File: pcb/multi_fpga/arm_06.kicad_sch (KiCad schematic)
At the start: 16 parts, among them U49 IM72D128V01XTMA1, U50 IM72D128V01XTMA1, U51 IM72D128V01XTMA1, U52 IM72D128V01XTMA1, U53 IM72D128V01XTMA1, U54 IM72D128V01XTMA1, U55 IM72D128V01XTMA1, U56 IM72D128V01XTMA1

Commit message: Fixed library and power issues.
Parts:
- C49, C50, C51, C52, C53, C54, C55, C56: symbol C -> multi_fpga:C
- U49, U50, U51, U52, U53, U54, U55, U56: symbol IM72D128 -> multi_fpga:IM72D128

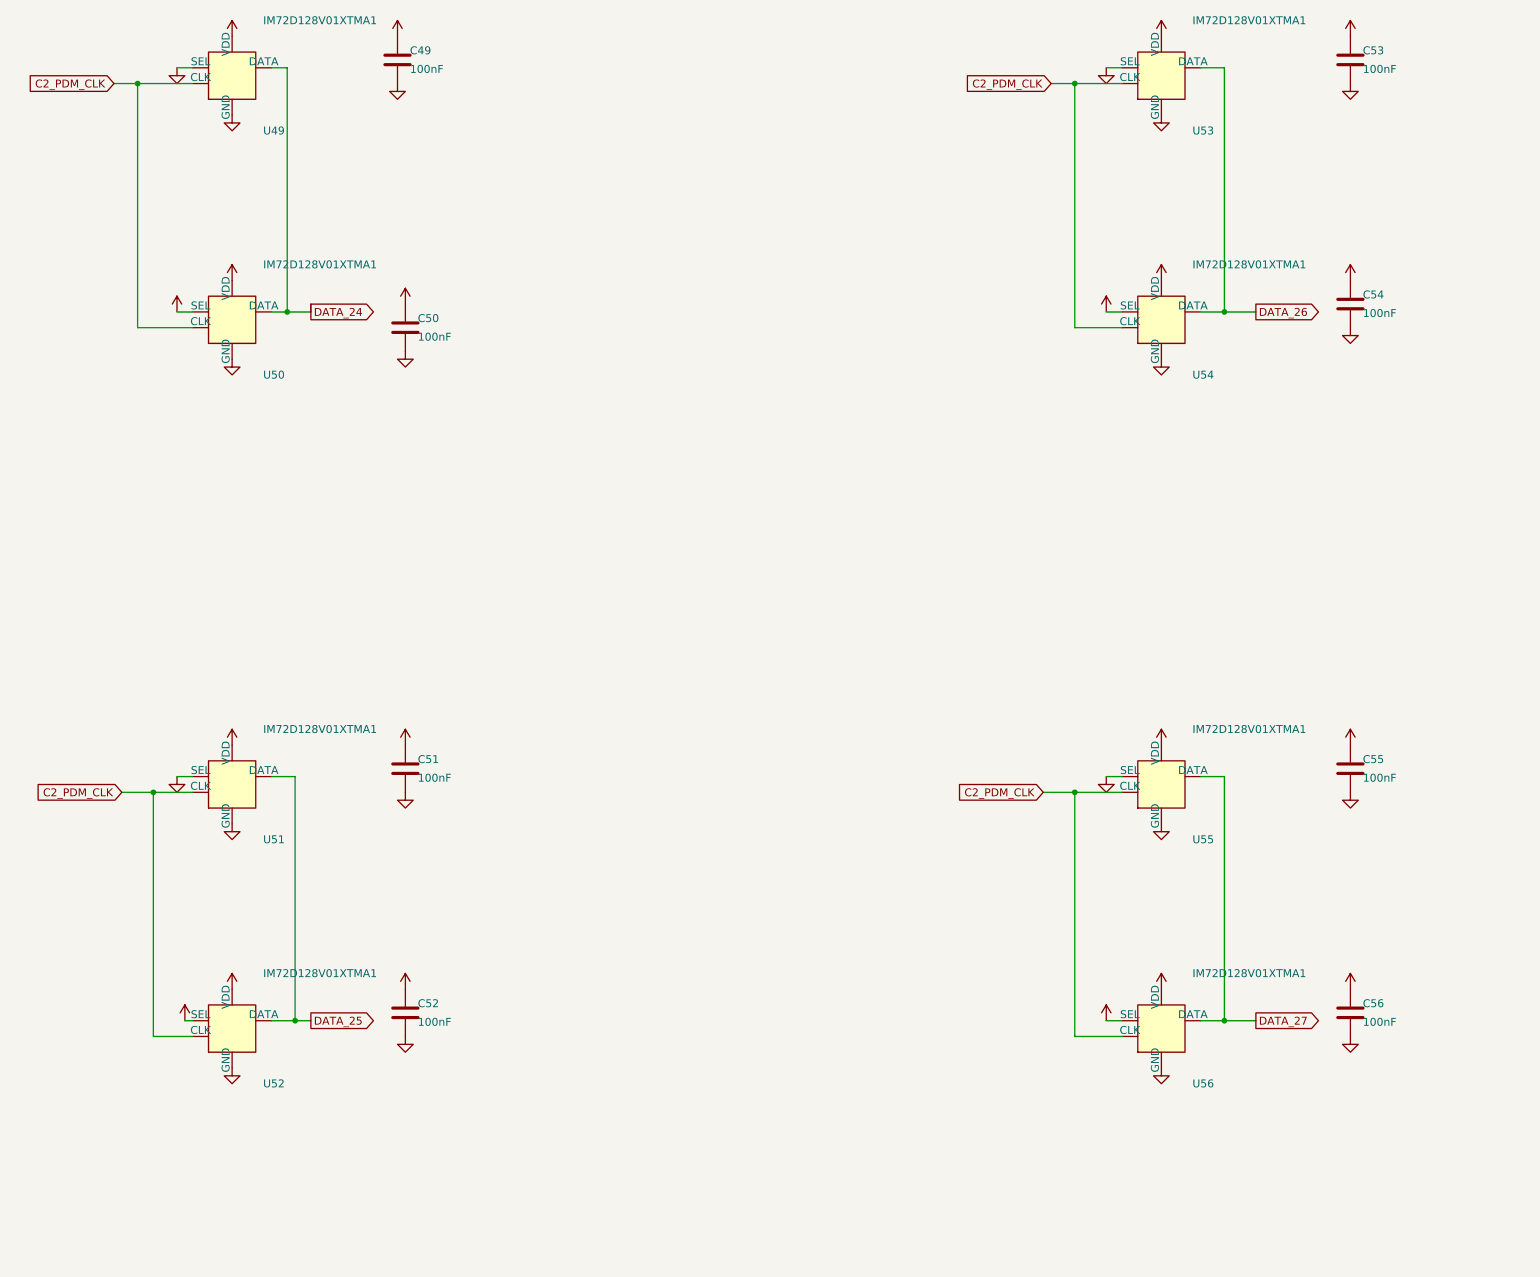
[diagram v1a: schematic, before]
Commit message: Fixed power and C ref des collisions.
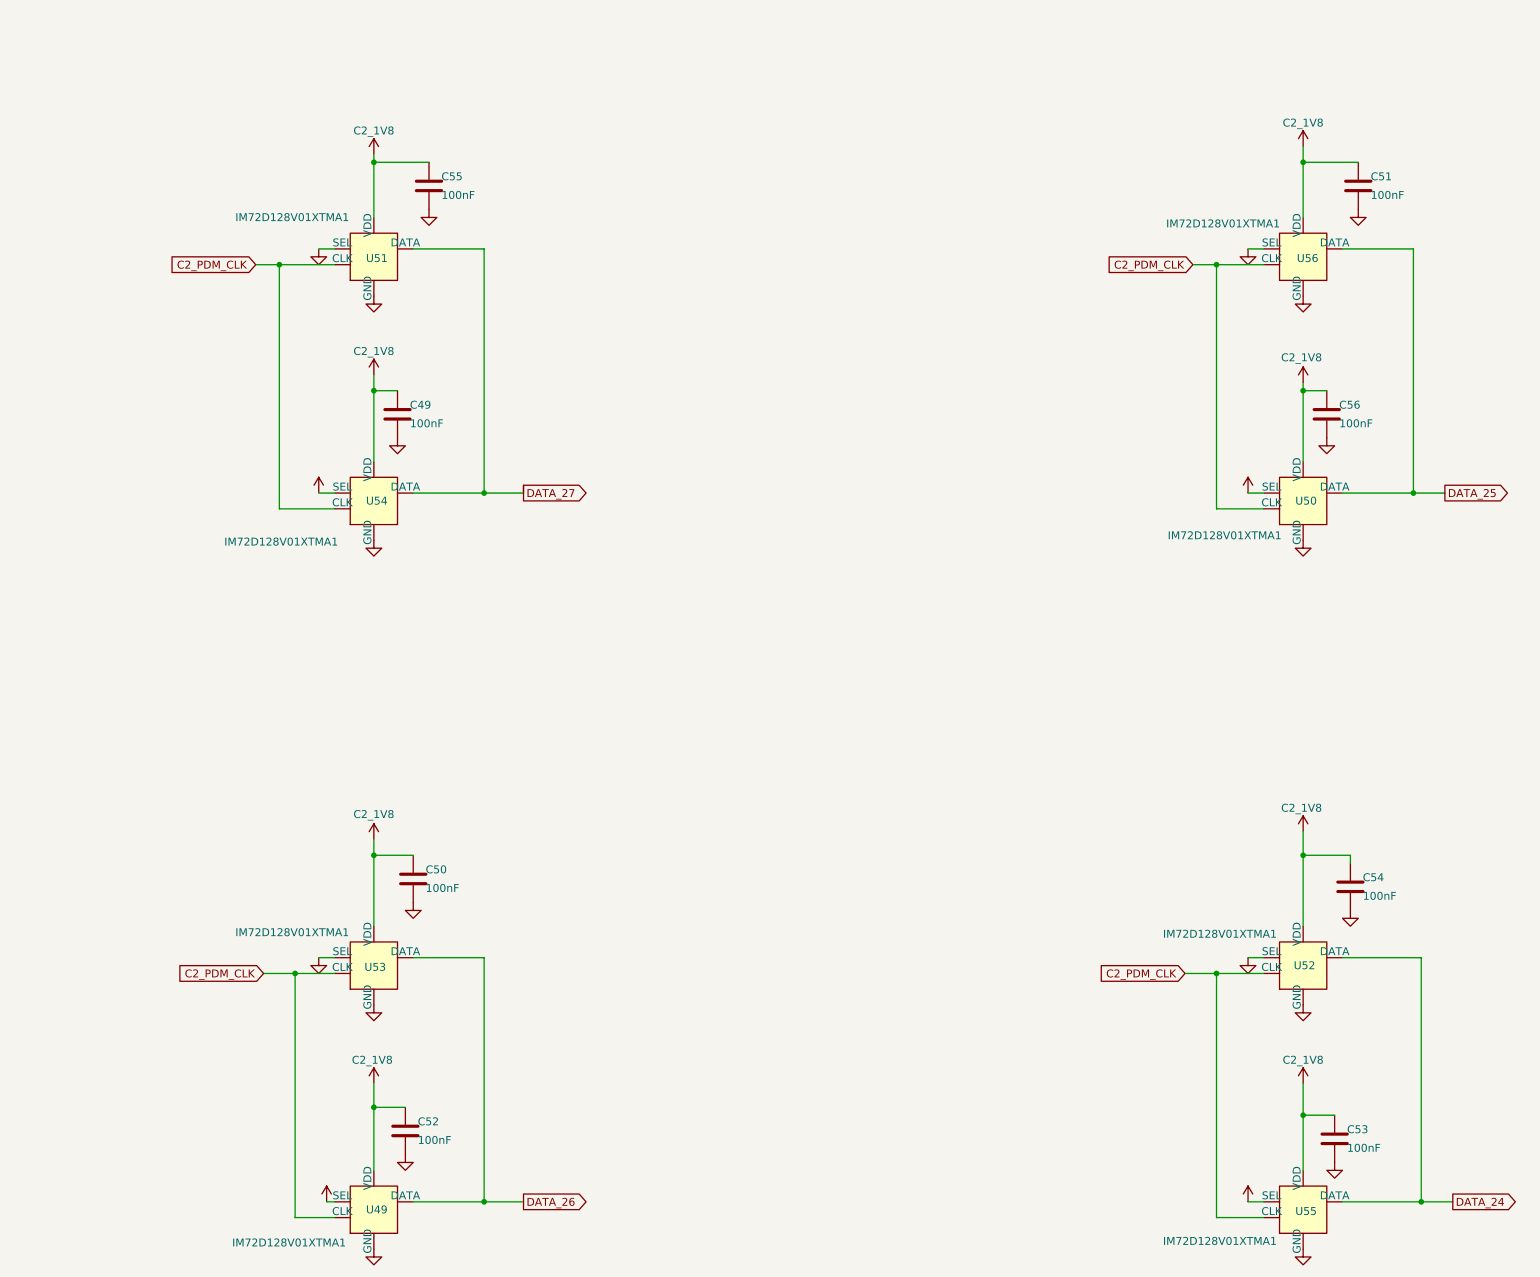
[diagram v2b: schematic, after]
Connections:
- net C2_1V8: now also U49.4 (SEL), U55.4 (SEL); no longer U52.4 (SEL), U56.4 (SEL)
- net DATA_24: now also U52.1 (DATA), U55.1 (DATA); no longer U49.1 (DATA), U50.1 (DATA)
- net DATA_25: now also U50.1 (DATA), U56.1 (DATA); no longer U51.1 (DATA), U52.1 (DATA)
- net DATA_26: now also U49.1 (DATA); no longer U54.1 (DATA)
- net DATA_27: now also U51.1 (DATA), U54.1 (DATA); no longer U55.1 (DATA), U56.1 (DATA)
- net GND: now also U52.4 (SEL), U56.4 (SEL); no longer U49.4 (SEL), U55.4 (SEL)

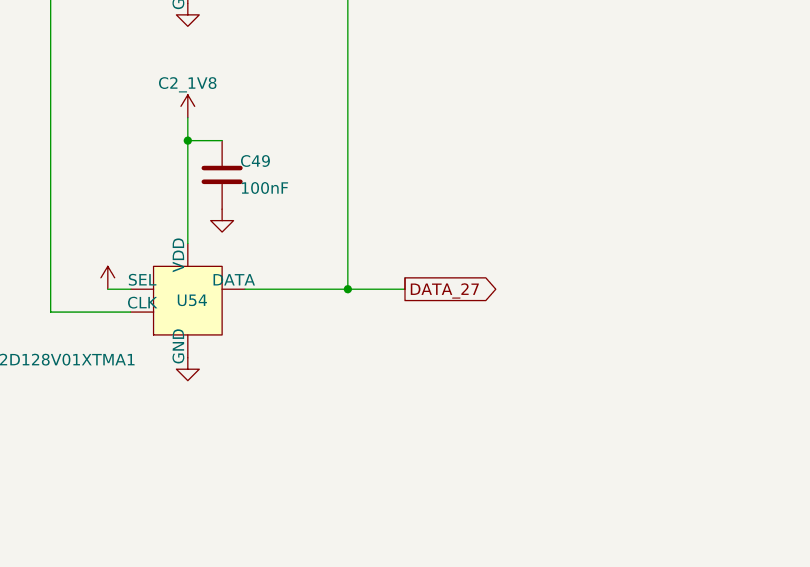
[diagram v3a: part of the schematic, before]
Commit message: Fixed regulator connection errors and dangling wire.
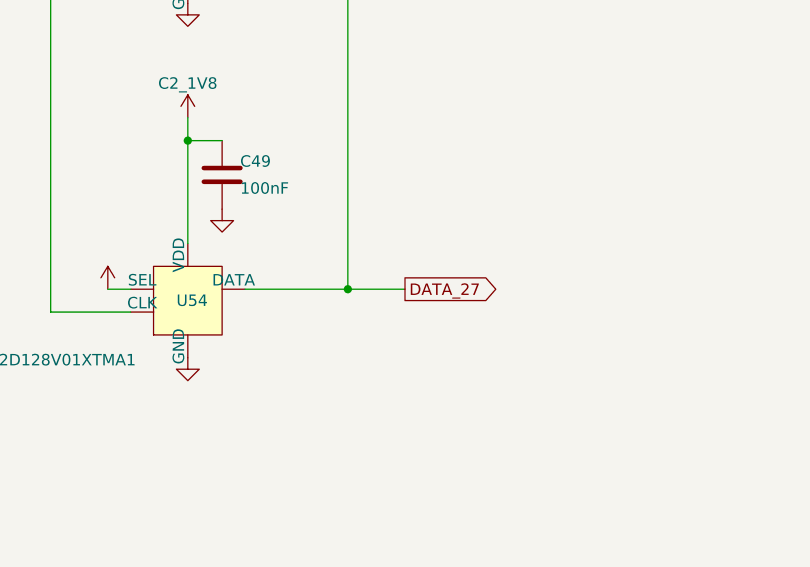
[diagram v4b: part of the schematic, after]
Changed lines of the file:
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@@
-	(wire
-		(pts
-			(xy 127 106.68) (xy 127 107.95)
-		)
-		(stroke
-			(width 0)
-			(type default)
-		)
-	)
 	(wire
 		(pts

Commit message: Global fix of res defs.
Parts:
- renumbered C49 to C66, C52 to C67, C50 to C68, C55 to C69, C56 to C70, C53 to C71, C54 to C72, C51 to C73, U51 to U49, U54 to U50, U53 to U51, U49 to U52, U56 to U53, U50 to U54, U52 to U55, U55 to U56

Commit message: Changed to use generic cap symbols and footprints.
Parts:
- C66, C67, C68, C69, C70, C71, C72, C73: symbol multi_fpga:C -> Device:C
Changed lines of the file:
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@@
 	)
 	(symbol
-		(lib_id "multi_fpga:C")
+		(lib_id "Device:C")
 		(at 107.95 210.82 0)
 		(unit 1)
@@
 		)
 		(property "Footprint" ""
-			(at 107.95 210.82 0)
+			(at 108.9152 214.63 0)
 			(hide yes)
 			(show_name no)
@@
 			)
 		)
-		(property "Description" ""
+		(property "Description" "Unpolarized capacitor"
 			(at 107.95 210.82 0)
 			(hide yes)
@@
 	)
 	(symbol
-		(lib_id "multi_fpga:C")
+		(lib_id "Device:C")
 		(at 257.81 212.09 0)
 		(unit 1)
@@
 		)
 		(property "Footprint" ""
-			(at 257.81 212.09 0)
+			(at 258.7752 215.9 0)
 			(hide yes)
 			(show_name no)
@@
 			)
 		)
-		(property "Description" ""
+		(property "Description" "Unpolarized capacitor"
 			(at 257.81 212.09 0)
 			(hide yes)
@@
 	)
 	(symbol
-		(lib_id "multi_fpga:C")
+		(lib_id "Device:C")
 		(at 106.68 95.25 0)
 		(unit 1)
@@
 		)
 		(property "Footprint" ""
-			(at 106.68 95.25 0)
+			(at 107.6452 99.06 0)
 			(hide yes)
 			(show_name no)
@@
 			)
 		)
-		(property "Description" ""
+		(property "Description" "Unpolarized capacitor"
 			(at 106.68 95.25 0)
 			(hide yes)
@@
 	)
 	(symbol
-		(lib_id "multi_fpga:C")
+		(lib_id "Device:C")
 		(at 261.62 58.42 0)
 		(unit 1)
@@
 		)
 		(property "Footprint" ""
-			(at 261.62 58.42 0)
+			(at 262.5852 62.23 0)
 			(hide yes)
 			(show_name no)
@@
 			)
 		)
-		(property "Description" ""
+		(property "Description" "Unpolarized capacitor"
 			(at 261.62 58.42 0)
 			(hide yes)
@@
 	)
 	(symbol
-		(lib_id "multi_fpga:C")
+		(lib_id "Device:C")
 		(at 109.22 170.18 0)
 		(unit 1)
@@
 		)
 		(property "Footprint" ""
-			(at 109.22 170.18 0)
+			(at 110.1852 173.99 0)
 			(hide yes)
 			(show_name no)
@@
 			)
 		)
-		(property "Description" ""
+		(property "Description" "Unpolarized capacitor"
 			(at 109.22 170.18 0)
 			(hide yes)
@@
 	)
 	(symbol
-		(lib_id "multi_fpga:C")
+		(lib_id "Device:C")
 		(at 260.35 171.45 0)
 		(unit 1)
@@
 		)
 		(property "Footprint" ""
-			(at 260.35 171.45 0)
+			(at 261.3152 175.26 0)
 			(hide yes)
 			(show_name no)
@@
 			)
 		)
-		(property "Description" ""
+		(property "Description" "Unpolarized capacitor"
 			(at 260.35 171.45 0)
 			(hide yes)
@@
 	)
 	(symbol
-		(lib_id "multi_fpga:C")
+		(lib_id "Device:C")
 		(at 256.54 95.25 0)
 		(unit 1)
@@
 		)
 		(property "Footprint" ""
-			(at 256.54 95.25 0)
+			(at 257.5052 99.06 0)
 			(hide yes)
 			(show_name no)
@@
 			)
 		)
-		(property "Description" ""
+		(property "Description" "Unpolarized capacitor"
 			(at 256.54 95.25 0)
 			(hide yes)
@@
 	)
 	(symbol
-		(lib_id "multi_fpga:C")
+		(lib_id "Device:C")
 		(at 111.76 58.42 0)
 		(unit 1)
@@
 		)
 		(property "Footprint" ""
-			(at 111.76 58.42 0)
+			(at 112.7252 62.23 0)
 			(hide yes)
 			(show_name no)
@@
 			)
 		)
-		(property "Description" ""
+		(property "Description" "Unpolarized capacitor"
 			(at 111.76 58.42 0)
 			(hide yes)

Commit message: Added stock footprints for C symbols.
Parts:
- C66, C67, C68, C69, C70, C71, C72, C73: footprint (none) -> Capacitor_SMD:C_0603_1608Metric
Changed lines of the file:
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@@
 			)
 		)
-		(property "Footprint" ""
+		(property "Footprint" "Capacitor_SMD:C_0603_1608Metric"
 			(at 108.9152 214.63 0)
 			(hide yes)
@@
 			)
 		)
-		(property "Footprint" ""
+		(property "Footprint" "Capacitor_SMD:C_0603_1608Metric"
 			(at 258.7752 215.9 0)
 			(hide yes)
@@
 			)
 		)
-		(property "Footprint" ""
+		(property "Footprint" "Capacitor_SMD:C_0603_1608Metric"
 			(at 107.6452 99.06 0)
 			(hide yes)
@@
 			)
 		)
-		(property "Footprint" ""
+		(property "Footprint" "Capacitor_SMD:C_0603_1608Metric"
 			(at 262.5852 62.23 0)
 			(hide yes)
@@
 			)
 		)
-		(property "Footprint" ""
+		(property "Footprint" "Capacitor_SMD:C_0603_1608Metric"
 			(at 110.1852 173.99 0)
 			(hide yes)
@@
 			)
 		)
-		(property "Footprint" ""
+		(property "Footprint" "Capacitor_SMD:C_0603_1608Metric"
 			(at 261.3152 175.26 0)
 			(hide yes)
@@
 			)
 		)
-		(property "Footprint" ""
+		(property "Footprint" "Capacitor_SMD:C_0603_1608Metric"
 			(at 257.5052 99.06 0)
 			(hide yes)
@@
 			)
 		)
-		(property "Footprint" ""
+		(property "Footprint" "Capacitor_SMD:C_0603_1608Metric"
 			(at 112.7252 62.23 0)
 			(hide yes)
